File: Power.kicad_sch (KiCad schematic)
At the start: 24 parts, among them J1 Conn_02x04_Odd_Even, U1 BL8028CB5TR, U2 BL8028CB5TR, U3 BL8028CB5TR

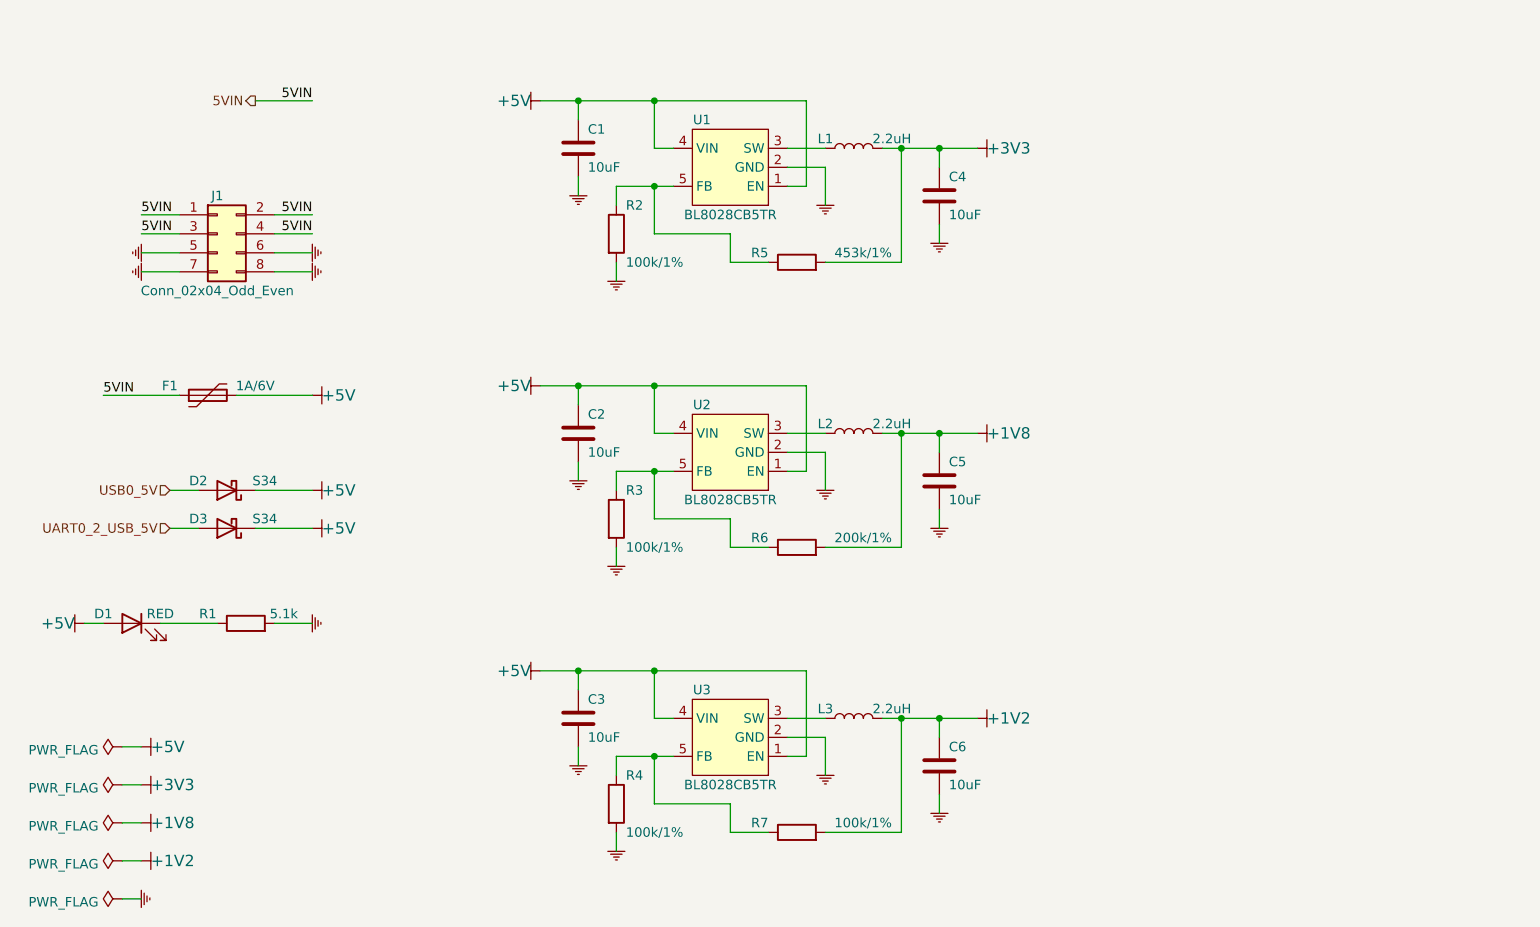
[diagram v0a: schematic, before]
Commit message: update schematic and footprints
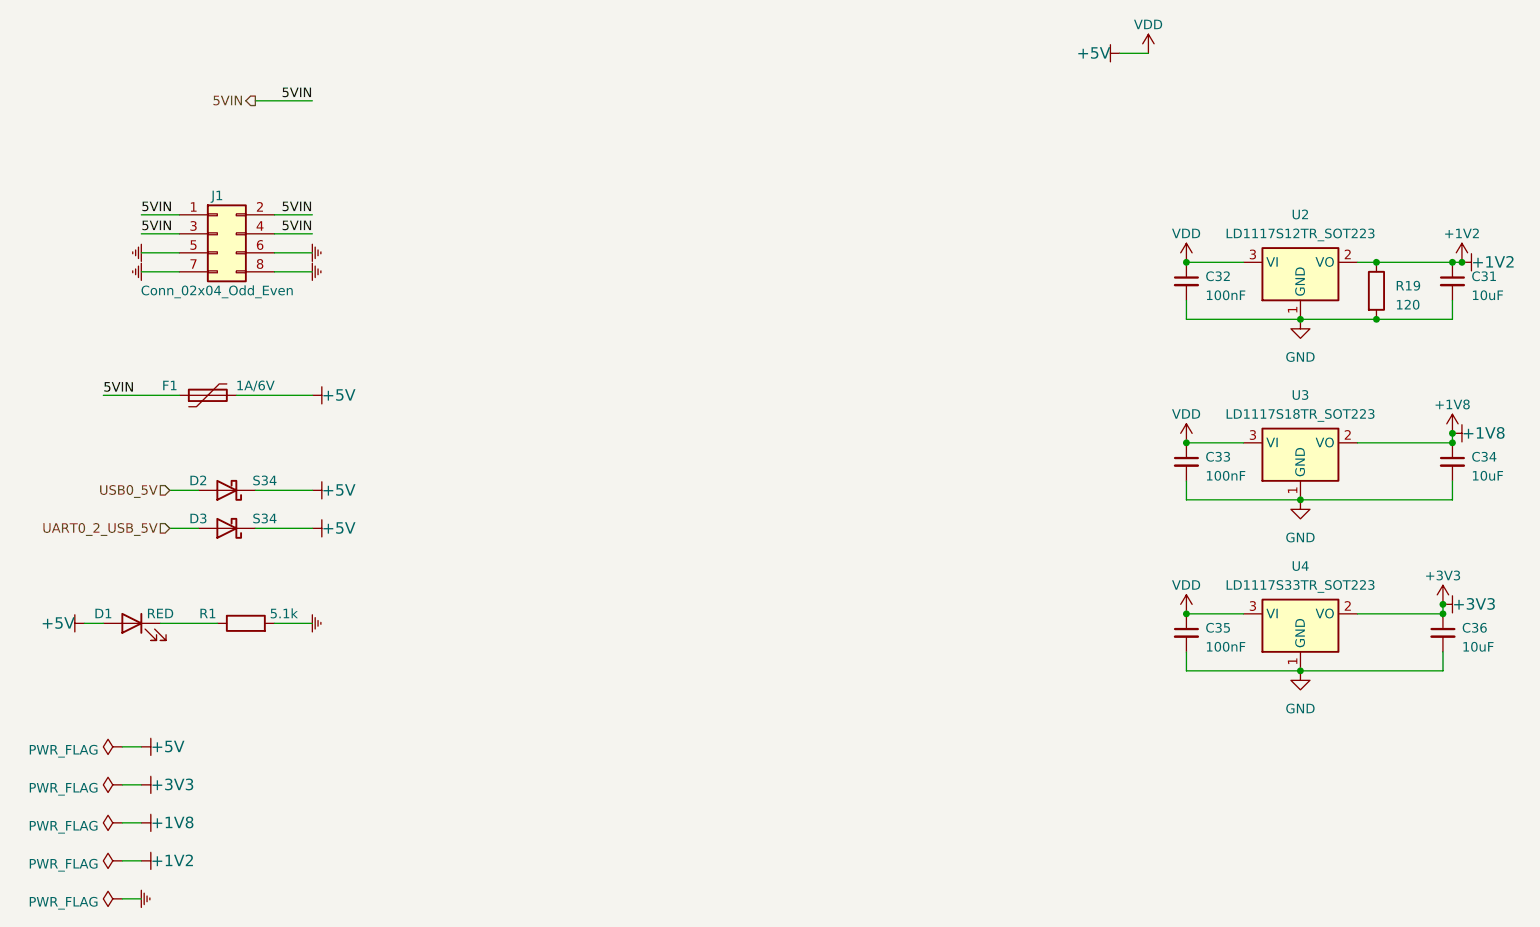
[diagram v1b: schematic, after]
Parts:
- removed C1, C2, C3, C4, C5, C6: 10uF, Capacitor_SMD:C_0805_2012Metric, symbol Device:C
- removed L1, L2, L3: 2.2uH, 0_ungrouped:Inductor_SMD_2520_2.5x2.0mm, symbol Device:L
- removed R2, R3, R4, R7: 100k/1%, Resistor_SMD:R_0603_1608Metric, symbol Device:R
- removed R5: 453k/1%, Resistor_SMD:R_0603_1608Metric, symbol Device:R
- removed R6: 200k/1%, Resistor_SMD:R_0603_1608Metric, symbol Device:R
- removed U1, U2, U3: BL8028CB5TR, Package_TO_SOT_SMD:SOT-23-5, symbol 0_ungrouped:BL8028CB5TR
- added C31, C34, C36: 10uF, Capacitor_SMD:C_0603_1608Metric_Pad1.08x0.95mm_HandSolder, symbol Device:C_Small
- added C32, C33, C35: 100nF, Capacitor_SMD:C_0603_1608Metric_Pad1.08x0.95mm_HandSolder, symbol Device:C_Small
- added R19: 120, Resistor_SMD:R_0603_1608Metric_Pad0.98x0.95mm_HandSolder, symbol Device:R
- added U2: LD1117S12TR_SOT223, Package_TO_SOT_SMD:SOT-223-3_TabPin2, symbol Regulator_Linear:LD1117S12TR_SOT223
- added U3: LD1117S18TR_SOT223, Package_TO_SOT_SMD:SOT-223-3_TabPin2, symbol Regulator_Linear:LD1117S18TR_SOT223
- added U4: LD1117S33TR_SOT223, Package_TO_SOT_SMD:SOT-223-3_TabPin2, symbol Regulator_Linear:LD1117S33TR_SOT223
- R1: footprint Resistor_SMD:R_0603_1608Metric -> Resistor_SMD:R_0805_2012Metric_Pad1.20x1.40mm_HandSolder
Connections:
- net +1V2: now also C31.1, R19.1, U2.2 (VO)
- net +1V8: now also C34.1, U3.2 (VO)
- net +3V3: now also C36.1, U4.2 (VO)
- net +5V: now also C32.1, C33.1, C35.1, U2.3 (VI), U3.3 (VI), U4.3 (VI)
- net GND: now also C31.2, C32.2, C33.2, C34.2, C35.2, C36.2, R19.2, U2.1 (GND), U3.1 (GND), U4.1 (GND)
